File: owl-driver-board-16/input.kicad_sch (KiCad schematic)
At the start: 7 parts, among them J3 1890963, Q1 AGM60P85AP

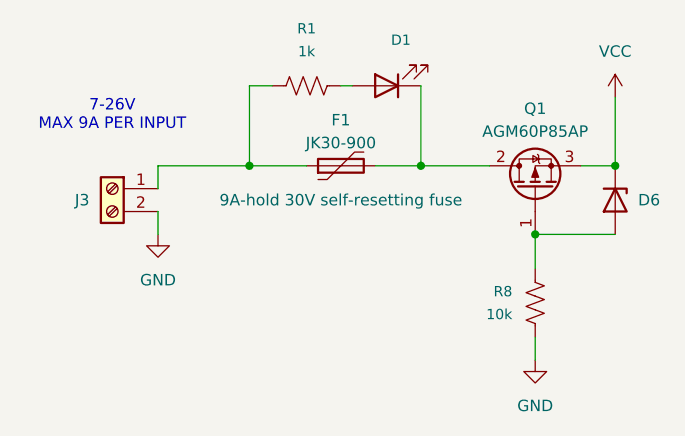
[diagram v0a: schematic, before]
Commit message: add a 16-way version
Add a 16-way version of the HAT. Drop the PWM controller to focus on
GPIO control of 16 outputs, with output enable/e-stop, and keeping the
25W Pi power supply.

This version (v1.0) has a small bug in the panel, fixed in v1.1.
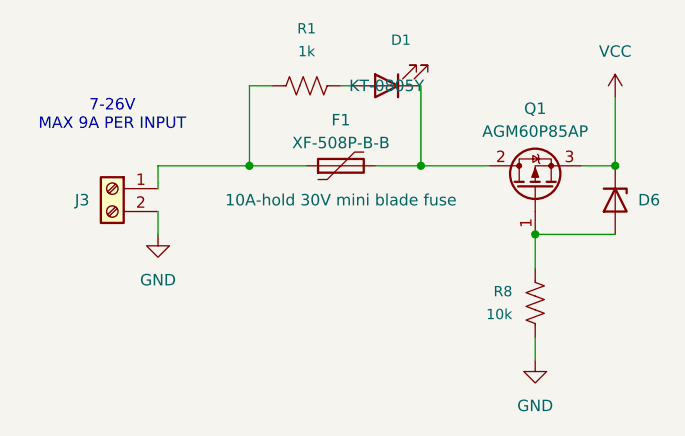
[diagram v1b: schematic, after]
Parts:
- D1: value SZYY0805R -> KT-0805Y; LCSC C434431 -> C2296; Part (none) -> KT-0805Y
- F1: value JK30-900 -> XF-508P-B-B; footprint Fuse:Fuse_Bourns_MF-RHT1000 -> Fuse:Fuseholder_Blade_Mini_Keystone_3568; LCSC C369112 -> C19727305; Note 9A-hold 30V self-resetting fuse -> 10A-hold 30V mini blade fuse
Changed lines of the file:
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@@
 			)
 		)
-		(property "Value" "JK30-900"
+		(property "Value" "XF-508P-B-B"
 			(at 157.48 87.63 90)
 			(effects
@@
 			)
 		)
-		(property "Footprint" "Fuse:Fuse_Bourns_MF-RHT1000"
+		(property "Footprint" "Fuse:Fuseholder_Blade_Mini_Keystone_3568"
 			(at 162.56 88.9 0)
 			(effects
@@
 			)
 		)
-		(property "Datasheet" "https://www.lcsc.com/datasheet/lcsc_datasheet_2304140030_Jinrui-Electronic-Materials-Co--JK30-900_C369112.pdf"
+		(property "Datasheet" "https://www.lcsc.com/datasheet/lcsc_datasheet_2410121830_XFCN-XF-508P-B-B_C19727305.pdf"
 			(at 157.48 90.17 0)
 			(effects
@@
 			)
 		)
-		(property "Note" "9A-hold 30V self-resetting fuse"
+		(property "Note" "10A-hold 30V mini blade fuse"
 			(at 157.48 93.98 90)
 			(effects
@@
 			)
 		)
-		(property "LCSC" "C369112"
+		(property "LCSC" "C19727305"
 			(at 157.48 90.17 0)
 			(effects
@@
 			)
 		)
-		(property "Value" "SZYY0805R"
+		(property "Value" "KT-0805Y"
 			(at 160.2815 79.629 90)
 			(effects
@@
 			)
 		)
-		(property "LCSC" "C434431"
-			(at 162.56 81.28 0)
-			(effects
-				(font
-					(size 1.27 1.27)
-				)
-				(hide yes)
-			)
-		)
+		(property "LCSC" "C2296"
+			(at 162.56 81.28 0)
+			(effects
+				(font
+					(size 1.27 1.27)
+				)
+				(hide yes)
+			)
+		)
+		(property "Part" "KT-0805Y"
+			(at 162.56 81.28 0)
+			(effects
+				(font
+					(size 1.27 1.27)
+				)
+			)
+		)
